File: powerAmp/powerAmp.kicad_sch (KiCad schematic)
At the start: 0 parts

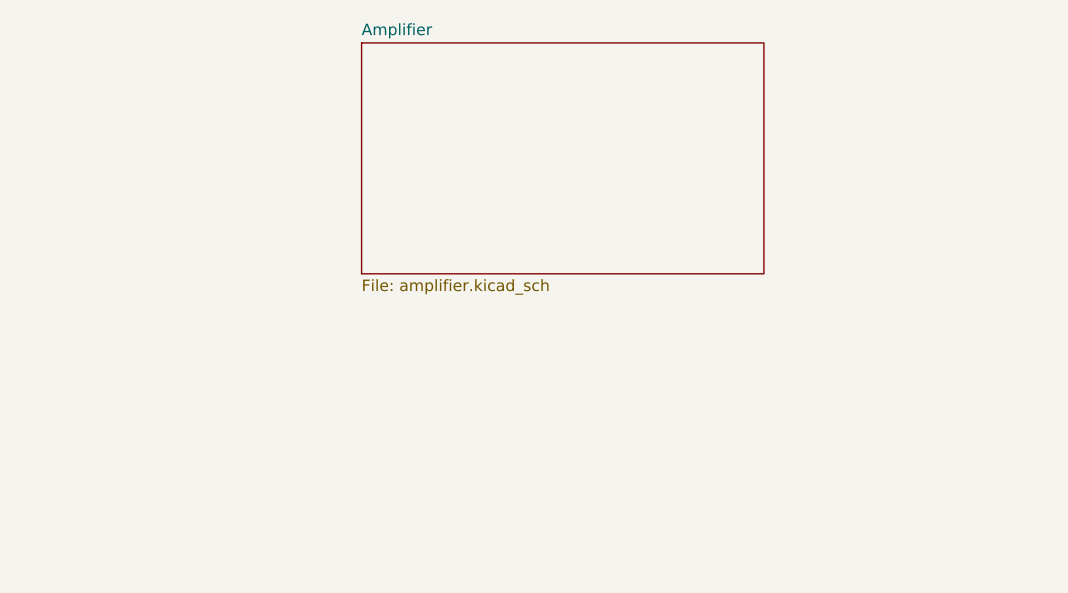
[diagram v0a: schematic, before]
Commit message: Added QEX power amp
Added project for the QEX power amplifier experiment board.
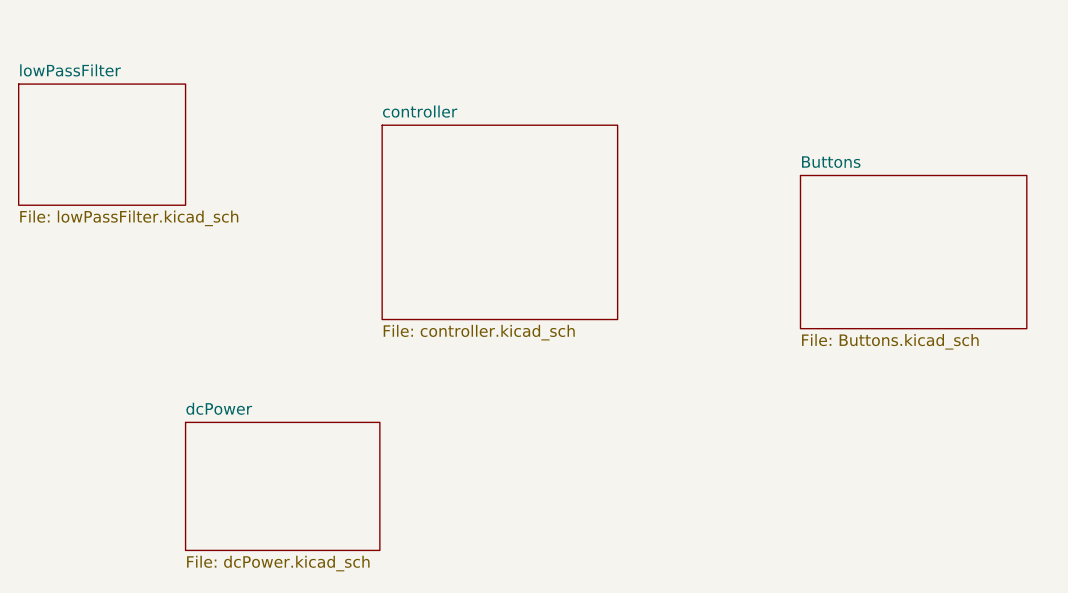
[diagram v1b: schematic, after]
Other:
- removed sheet Amplifier
- added sheet Buttons (Buttons.kicad_sch)
- added sheet controller (controller.kicad_sch)
- added sheet dcPower (dcPower.kicad_sch)
- added sheet lowPassFilter (lowPassFilter.kicad_sch)
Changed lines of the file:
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@@
 (kicad_sch (version 20230121) (generator eeschema)
   (paper "A4")
-  (sheet (at 60.706 26.67) (size 44.704 25.654) (fields_autoplaced)
+  (sheet (at 109.474 41.402) (size 25.146 17.018) (fields_autoplaced)
     (stroke (width 0.1524) (type solid))
     (fill (color 0 0 0 0.0000))
-    (property "Sheetname" "Amplifier" (at 60.706 25.9584 0)
+    (property "Sheetname" "Buttons" (at 109.474 40.6904 0)
       (effects (font (size 1.27 1.27)) (justify left bottom))
     )
-    (property "Sheetfile" "amplifier.kicad_sch" (at 60.706 52.9086 0)
+    (property "Sheetfile" "Buttons.kicad_sch" (at 109.474 59.0046 0)
       (effects (font (size 1.27 1.27)) (justify left top))
     )
+    (instances
+      (project "powerAmp"
+        (path "/5c7fcd87-e9b0-4f6c-8f25-d414a19db244" (page "5"))
+      )
+    )
+  )
+  (sheet (at 41.148 68.834) (size 21.59 14.224) (fields_autoplaced)
+    (stroke (width 0.1524) (type solid))
+    (fill (color 0 0 0 0.0000))
+    (property "Sheetname" "dcPower" (at 41.148 68.1224 0)
+      (effects (font (size 1.27 1.27)) (justify left bottom))
+    )
+    (property "Sheetfile" "dcPower.kicad_sch" (at 41.148 83.6426 0)
+      (effects (font (size 1.27 1.27)) (justify left top))
+    )
+    (instances
+      (project "powerAmp"
+        (path "/5c7fcd87-e9b0-4f6c-8f25-d414a19db244" (page "3"))
+      )
+    )
+  )
+  (sheet (at 22.606 31.242) (size 18.542 13.462) (fields_autoplaced)
+    (stroke (width 0.1524) (type solid))
+    (fill (color 0 0 0 0.0000))
+    (property "Sheetname" "lowPassFilter" (at 22.606 30.5304 0)
+      (effects (font (size 1.27 1.27)) (justify left bottom))
+    )
+    (property "Sheetfile" "lowPassFilter.kicad_sch" (at 22.606 45.2886 0)
+      (effects (font (size 1.27 1.27)) (justify left top))
+    )
+    (instances
+      (project "powerAmp"
+        (path "/5c7fcd87-e9b0-4f6c-8f25-d414a19db244" (page "4"))
+      )
+    )
+  )
+  (sheet (at 62.992 35.814) (size 26.162 21.59) (fields_autoplaced)
+    (stroke (width 0.1524) (type solid))
+    (fill (color 0 0 0 0.0000))
+    (property "Sheetname" "controller" (at 62.992 35.1024 0)
+      (effects (font (size 1.27 1.27)) (justify left bottom))
+    )
+    (property "Sheetfile" "controller.kicad_sch" (at 62.992 57.9886 0)
+      (effects (font (size 1.27 1.27)) (justify left top))
+    )
